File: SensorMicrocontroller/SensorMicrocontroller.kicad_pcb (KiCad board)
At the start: 2 copper layers, 100 x 100 mm, 40 parts, among them J1 JST B4B-PH-SM4-TB, J2 JST B4B-PH-SM4-TB, J3 JST B6B-PH-SM4-TB, J4 JST B4B-PH-SM4-TB, J5 JST B4B-PH-SM4-TB, J8 12V Connector, J9 Light Connector, Q1 DMT6009LCT, Q2 DMT6009LCT, U1 ADS1115IDGS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

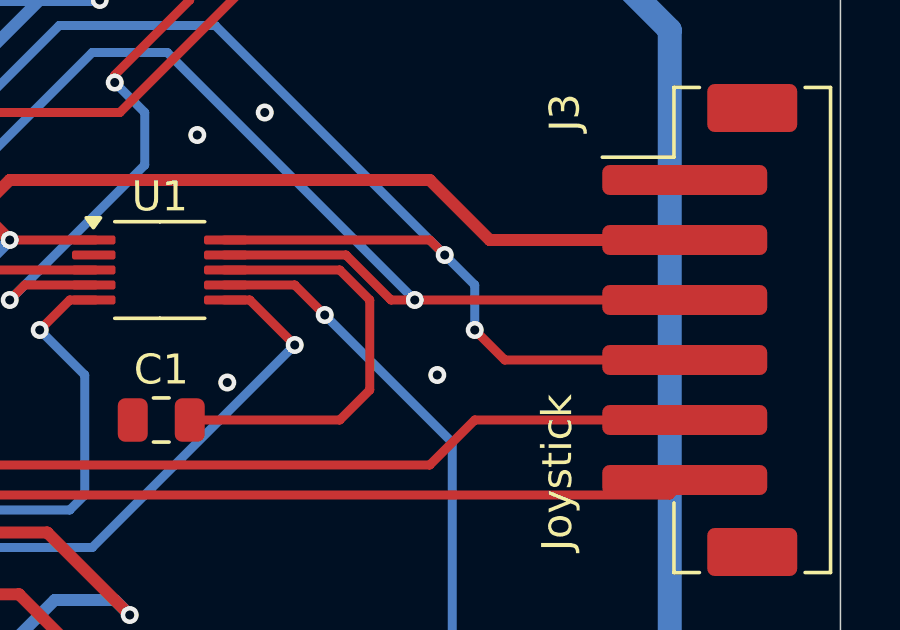
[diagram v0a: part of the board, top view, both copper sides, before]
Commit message: Fixed power error on ADC
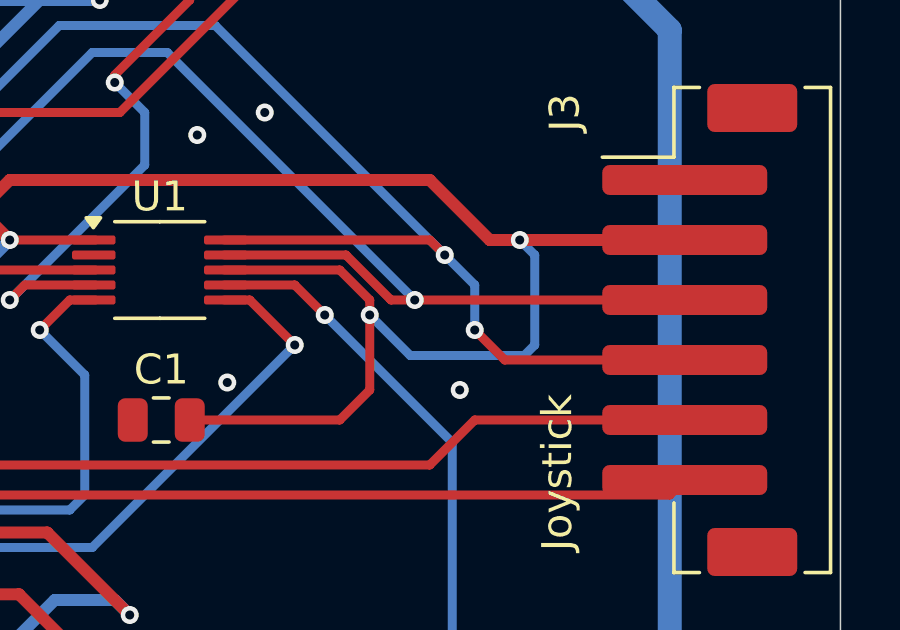
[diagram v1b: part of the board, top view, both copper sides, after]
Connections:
- C1 pad 2: Net-(U1-VDD) -> /3.3V
- U1 pad 8: Net-(U1-VDD) -> /3.3V
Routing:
- net /3.3V: track 344.2 -> 368.8 mm, vias 14 -> 16
- net Net-(U1-VDD): track 14.7 -> 0.00 mm

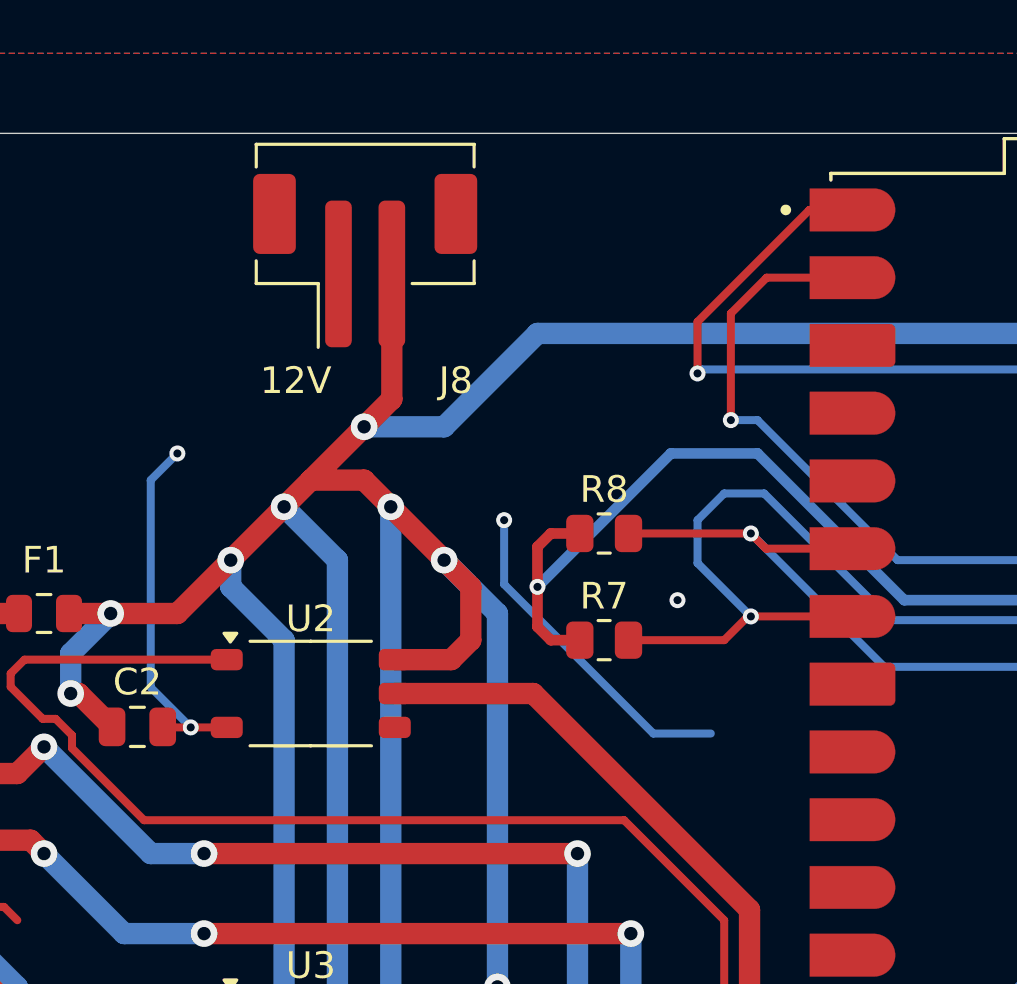
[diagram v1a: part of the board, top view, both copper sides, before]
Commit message: Added LiDAR power controller
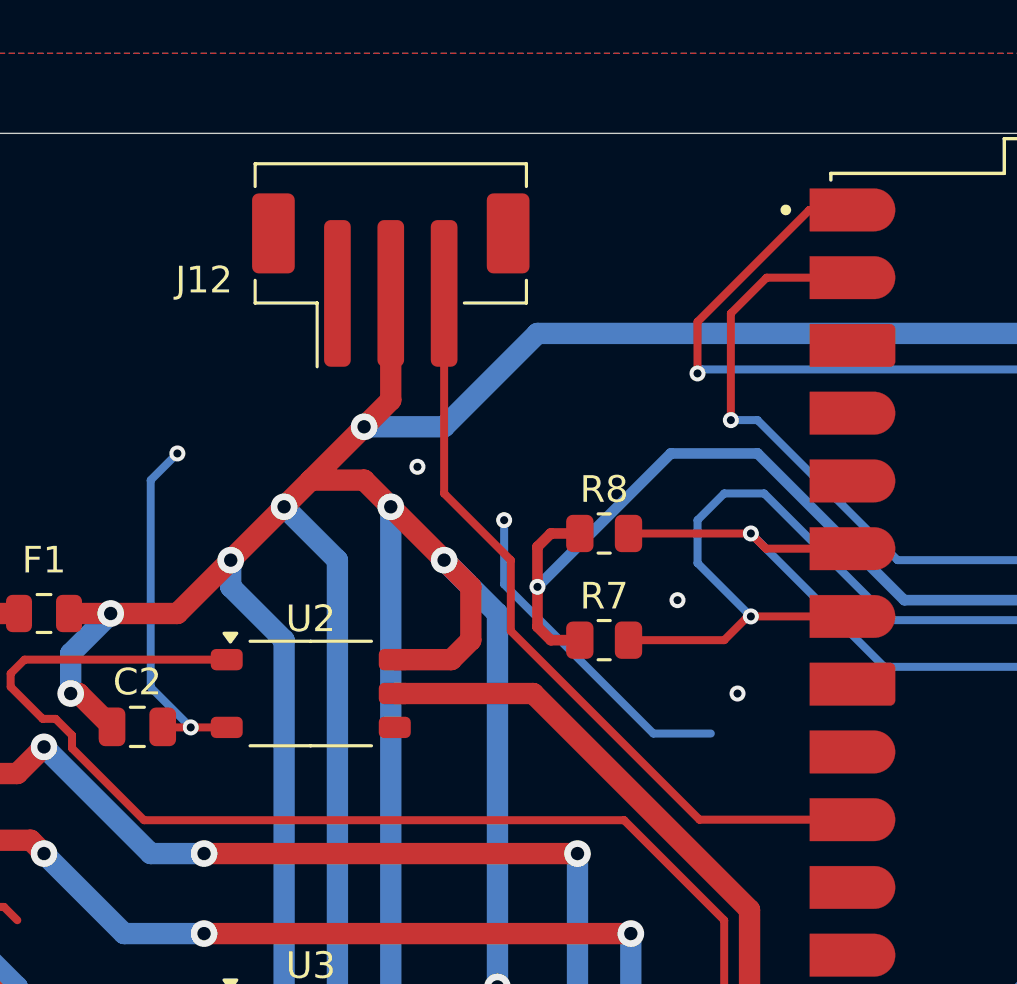
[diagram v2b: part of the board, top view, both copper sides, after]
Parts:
- removed J8: 12V Connector, Connector_JST:JST_PH_B2B-PH-SM4-TB_1x02-1MP_P2.00mm_Vertical
- added J12: 12V Connector, Connector_JST:JST_PH_B3B-PH-SM4-TB_1x03-1MP_P2.00mm_Vertical, F.Cu at (118.0, 53.5)
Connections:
- U4 pad 10: unconnected-(U4-GP7-Pad10) -> /LiDAR On Pin
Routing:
- net /LiDAR On Pin: track 0.00 -> 29.4 mm
- net /GND: vias 24 -> 26

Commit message: Updated board version number
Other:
- board text added: "Rev v1.1"
- board text removed: "Rev v1.0"

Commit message: Updated SensorMicrocontroller design
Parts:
- removed F1: Fuse, Fuse:Fuse_0805_2012Metric
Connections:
- J9 pad 4: /Light White Wire -> /12V
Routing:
- net /12V: track 521.2 -> 549.3 mm, vias 15 -> 17
- net /Light White Wire: track 26.2 -> 0.00 mm, vias 2 -> 0

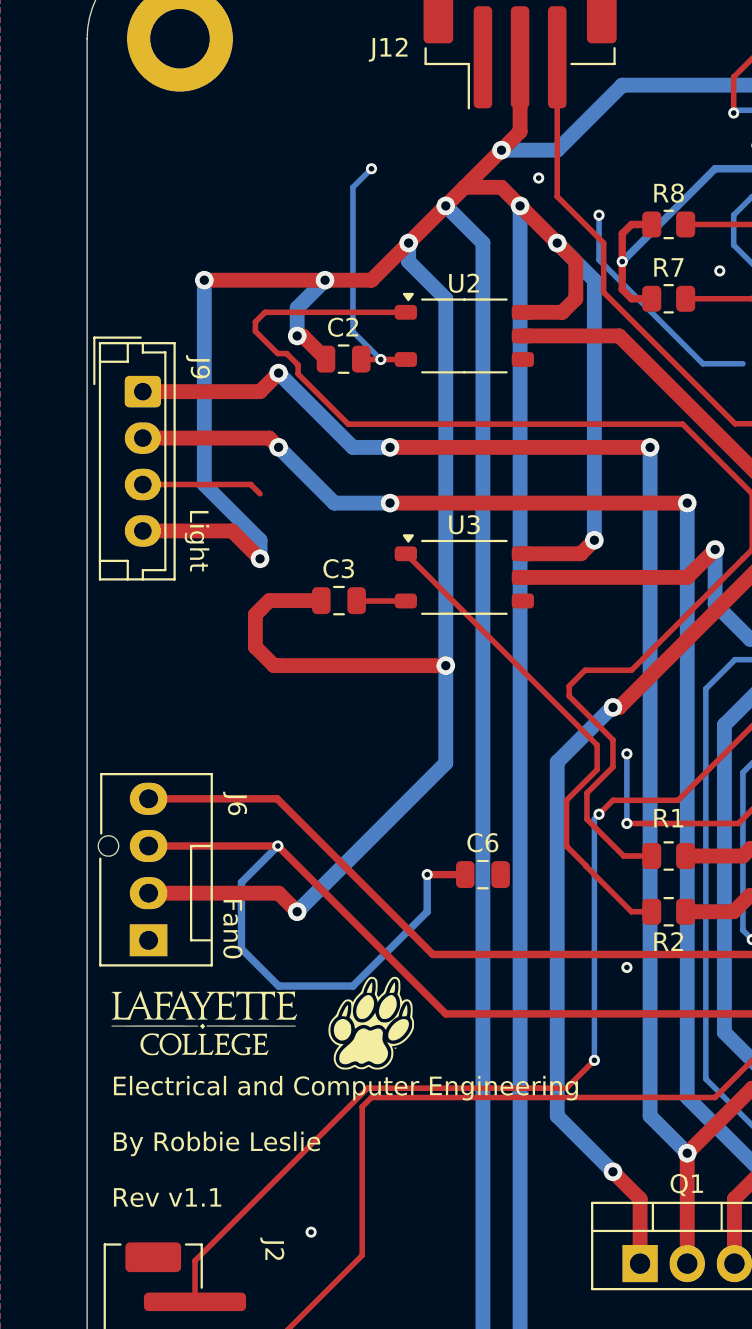
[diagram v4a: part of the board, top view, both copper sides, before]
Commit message: Fixed 12V silkscreen on sensor board
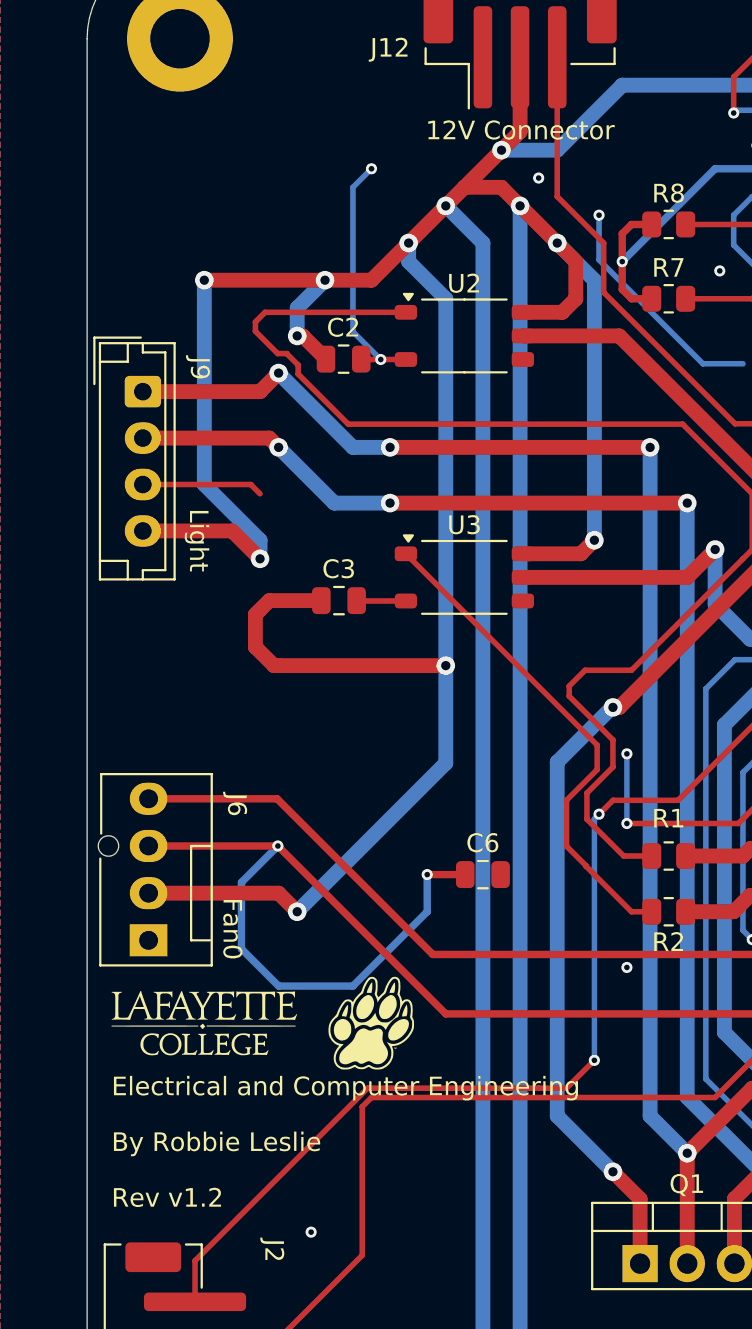
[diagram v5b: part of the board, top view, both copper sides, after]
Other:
- board text added: "Rev v1.2"
